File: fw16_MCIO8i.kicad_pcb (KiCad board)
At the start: 4 copper layers, 118.7 x 72.5 mm, 18 parts, among them U1 M24C32-FDW6TP

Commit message: Fixups
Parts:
- C1: value 0.1uF -> 1uF
- FAN_L1, FAN_R1: value FAN -> 59453-041110EDHLF
- MCIO1: value G97R22322HR -> G97R22312HR; footprint mcio-connector:AMPHENOL_G97R22322HR -> mcio-connector:AMPHENOL_G97R22312HR
- R1, R2: value 330 -> 330kΩ
- R3, R50, R51: value 10K -> 10kΩ
- R4: value 100k -> 100kΩ
- TP3, TP5: footprint TestPoint:TestPoint_Pad_D1.0mm -> TestPoint:TestPoint_Pad_D3.0mm
- moved MCIO1 0.56 mm to (134.2, 31.2)
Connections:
- FXBeam1 pad SA5: unconnected-(FXBeam1-PEX_RST#-PadSA5) -> /PEX_RST
- FXBeam1 pad SC2: unconnected-(FXBeam1-PEX_REFCLK-PadSC2) -> /PEX_CLK+
- FXBeam1 pad SD2: unconnected-(FXBeam1-PEX_REFCLK#-PadSD2) -> /PEX_CLK-
- MCIO1 pad A11: unconnected-(MCIO1-PCI0_RST-PadA11) -> /PEX_CLK+
- MCIO1 pad A12: unconnected-(MCIO1-PadA12) -> /PEX_CLK-
- MCIO1 pad A14: /TX2+ -> /RX2+
- MCIO1 pad A15: /TX2- -> /RX2-
- MCIO1 pad A17: /TX3+ -> /RX3+
- MCIO1 pad A18: /TX3- -> /RX3-
- MCIO1 pad A2: /TX0+ -> /RX0+
- MCIO1 pad A20: /TX4+ -> /RX4+
- MCIO1 pad A21: /TX4- -> /RX4-
- MCIO1 pad A23: /TX5+ -> /RX5+
- MCIO1 pad A24: /TX5- -> /RX5-
- MCIO1 pad A3: /TX0- -> /RX0-
- MCIO1 pad A32: /TX6+ -> /RX6+
- MCIO1 pad A33: /TX6- -> /RX6-
- MCIO1 pad A35: /TX7+ -> /RX7+
- MCIO1 pad A36: /TX7- -> /RX7-
- MCIO1 pad A5: /TX1+ -> /RX1+
- MCIO1 pad A6: /TX1- -> /RX1-
- MCIO1 pad B11: unconnected-(MCIO1-CLK0+-PadB11) -> /PEX_RST
- MCIO1 pad B14: /RX2+ -> /TX2+
- MCIO1 pad B15: /RX2- -> /TX2-
- MCIO1 pad B17: /RX3+ -> /TX3+
- MCIO1 pad B18: /RX3- -> /TX3-
- MCIO1 pad B2: /RX0+ -> /TX0+
- MCIO1 pad B20: /RX4+ -> /TX4+
- MCIO1 pad B21: /RX4- -> /TX4-
- MCIO1 pad B23: /RX5+ -> /TX5+
- MCIO1 pad B24: /RX5- -> /TX5-
- MCIO1 pad B3: /RX0- -> /TX0-
- MCIO1 pad B32: /RX6+ -> /TX6+
- MCIO1 pad B33: /RX6- -> /TX6-
- MCIO1 pad B35: /RX7+ -> /TX7+
- MCIO1 pad B36: /RX7- -> /TX7-
- MCIO1 pad B5: /RX1+ -> /TX1+
- MCIO1 pad B6: /RX1- -> /TX1-
- R1 pad 2: Net-(FXBeam1-ID0) -> Net-(R1-Pad2)
- R2 pad 2: Net-(FXBeam1-ID1) -> Net-(R2-Pad2)
- R3 pad 2: Net-(U1-WC) -> Net-(R3-Pad2)
- R4 pad 2: Net-(U1-WC) -> Net-(R3-Pad2)
- TP3 pad 1: Net-(FXBeam1-ID1) -> Net-(R2-Pad2)
- TP5 pad 1: Net-(FXBeam1-ID0) -> Net-(R1-Pad2)
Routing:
- net unconnected-(FXBeam1-PEX_RST#-PadSA5): track 33.0 -> 0.00 mm, vias 1 -> 0
- net /PEX_RST: track 0.00 -> 33.0 mm, vias 0 -> 1

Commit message: Fox
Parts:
- moved R2 65.7 mm to (144.7, 84.5), turned to 180 degrees
- moved TP3 59.4 mm to (141.0, 84.5)
- moved R1 57.2 mm to (78.5, 85.5)
- moved TP5 49.2 mm to (82.2, 85.5)
- moved C1 2.02 mm to (87.2, 75.8)
- moved R3 2.02 mm to (87.2, 77.0)
- moved R4 2.02 mm to (87.2, 78.0)
- moved R50 2.02 mm to (87.2, 79.2)
- moved R51 2.02 mm to (87.2, 80.2)
- renumbered U1 to EEPROM1, FXBeam1 to FXBEAM1
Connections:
- FXBEAM1 pad PJ1: Net-(FXBeam1-ID0) -> Net-(FXBEAM1-ID0)
- FXBEAM1 pad SL2: Net-(FXBeam1-ID1) -> Net-(FXBEAM1-ID1)
- R1 pad 2: Net-(R1-Pad2) -> Net-(FXBEAM1-ID0)
- R2 pad 2: Net-(R2-Pad2) -> Net-(FXBEAM1-ID1)
- TP3 pad 1: Net-(R2-Pad2) -> Net-(FXBEAM1-ID1)
- TP5 pad 1: Net-(R1-Pad2) -> Net-(FXBEAM1-ID0)
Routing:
- net GND: track 0.00 -> 818.4 mm, vias 0 -> 9
- net 12V_FAN: track 116.6 -> 0.00 mm
- net /RX1-: track 7.09 -> 68.3 mm, vias 1 -> 0
- net /RX1+: track 7.86 -> 68.2 mm, vias 1 -> 0
- net /TX0-: track 9.70 -> 68.2 mm, vias 0 -> 1
- net /TX0+: track 10.2 -> 68.2 mm, vias 0 -> 1
- net /RX2-: track 7.76 -> 64.0 mm
- net /RX2+: track 7.94 -> 64.0 mm
- net /FAN1_PWM: track 56.0 -> 0.00 mm, vias 2 -> 0
- net /RX0-: track 9.57 -> 65.4 mm
- net /TX5+: track 9.19 -> 64.9 mm
- net /RX3+: track 4.96 -> 60.6 mm
- net /RX3-: track 5.09 -> 60.5 mm
- net /RX0+: track 10.1 -> 63.9 mm
- net /FAN1_SPD: track 53.5 -> 0.00 mm, vias 2 -> 0
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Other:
- board text added: "Designed by Makuru and Love"
- board text removed: "Designed by Terrails"

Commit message: cat
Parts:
- removed R3: 10kΩ, PCM_JLCPCB:R_0402
- removed R4: 100kΩ, PCM_JLCPCB:R_0402
- moved C1 2.00 mm to (87.2, 77.8)
- moved EEPROM1 0.39 mm to (81.6, 78.8)
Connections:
- EEPROM1 pad 7: Net-(U1-WC) -> GND
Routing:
- net 12V_FAN: track 0.00 -> 111.4 mm, vias 0 -> 4
- net /FAN1_PWM: track 0.00 -> 59.5 mm
- net /FAN1_SPD: track 0.00 -> 57.3 mm, vias 0 -> 2
- net /FAN0_SPD: track 0.00 -> 51.6 mm, vias 0 -> 2
- net /PEX_RST: track 10.8 -> 62.0 mm
- net /FAN0_PWM: track 0.00 -> 46.1 mm, vias 0 -> 2
- net /TX6+: track 48.2 -> 83.7 mm, vias 1 -> 2
- net Net-(FXBEAM1-ID1): track 0.00 -> 34.9 mm, vias 0 -> 2
- net /TX6-: track 48.2 -> 82.3 mm, vias 1 -> 2
- net Net-(FXBEAM1-ID0): track 0.00 -> 32.7 mm, vias 0 -> 2
- net 3V3_ALW: track 0.00 -> 19.4 mm
- net /TX5+: track 64.9 -> 47.1 mm
- net /TX7+: track 43.4 -> 30.6 mm, vias 0 -> 1
- net /TX7-: track 43.3 -> 30.6 mm, vias 0 -> 1
- net /TX4-: track 57.9 -> 48.9 mm
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
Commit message: changed parts
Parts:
- FAN_L1, FAN_R1: value 59453-041110EDHLF -> F3011B7H111005E200; footprint fan-connector:AMPHENOL_59453-041110EDHLF -> fan-connector:AMPHENOL_F33D-1A7H1-E7C04
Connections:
- FAN_L1 pad 1: 12V_FAN -> GND
- FAN_L1 pad 2: /FAN0_SPD -> /FAN0_PWM
- FAN_L1 pad 3: /FAN0_PWM -> /FAN0_SPD
- FAN_L1 pad 4: GND -> 12V_FAN
- FAN_R1 pad 1: 12V_FAN -> GND
- FAN_R1 pad 2: /FAN1_SPD -> /FAN1_PWM
- FAN_R1 pad 3: /FAN1_PWM -> /FAN1_SPD
- FAN_R1 pad 4: GND -> 12V_FAN
- FXBEAM1 pad PC3: /I2C_SCL -> unconnected-(FXBEAM1-I2C_CLK_ALW-PadPC3)
- FXBEAM1 pad PF2: unconnected-(FXBEAM1-I2C_INT_ALW-PadPF2) -> /I2C_SCL
- FXBEAM1 pad PG2: unconnected-(FXBEAM1-I2C_INT_VS-PadPG2) -> /PE_SDA
- FXBEAM1 pad PG3: unconnected-(FXBEAM1-I2C_DAT_VS-PadPG3) -> /PE_SCL
- MCIO1 pad B8: unconnected-(MCIO1-SMSCL_A-PadB8) -> /PE_SCL
- MCIO1 pad B9: unconnected-(MCIO1-SMSDA_A-PadB9) -> /PE_SDA
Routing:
- net GND: track 821.0 -> 258.5 mm, vias 9 -> 36
- net /TX7-: track 30.6 -> 92.2 mm, vias 1 -> 2
- net /TX7+: track 30.6 -> 92.1 mm, vias 1 -> 2
- net /TX6+: track 83.7 -> 26.6 mm
- net /TX6-: track 82.3 -> 25.4 mm
- net /TX1+: track 0.00 -> 39.0 mm, vias 0 -> 1
- net /TX1-: track 0.00 -> 38.3 mm, vias 0 -> 1
- net /PEX_RST: track 62.0 -> 24.1 mm, vias 3 -> 1
- net /RX1-: track 68.3 -> 30.5 mm, vias 0 -> 1
- net /RX1+: track 68.2 -> 31.1 mm, vias 0 -> 1
- net /RX3-: track 60.5 -> 23.7 mm, vias 0 -> 1
- net /RX2-: track 64.0 -> 28.2 mm, vias 0 -> 1
- net /RX4+: track 55.5 -> 19.8 mm, vias 0 -> 1
- net /RX3+: track 60.5 -> 25.0 mm, vias 0 -> 1
- net /RX4-: track 55.5 -> 20.5 mm, vias 0 -> 1
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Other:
- board text added: "Designed by Makuru"
- board text removed: "Designed by Makuru and Love"

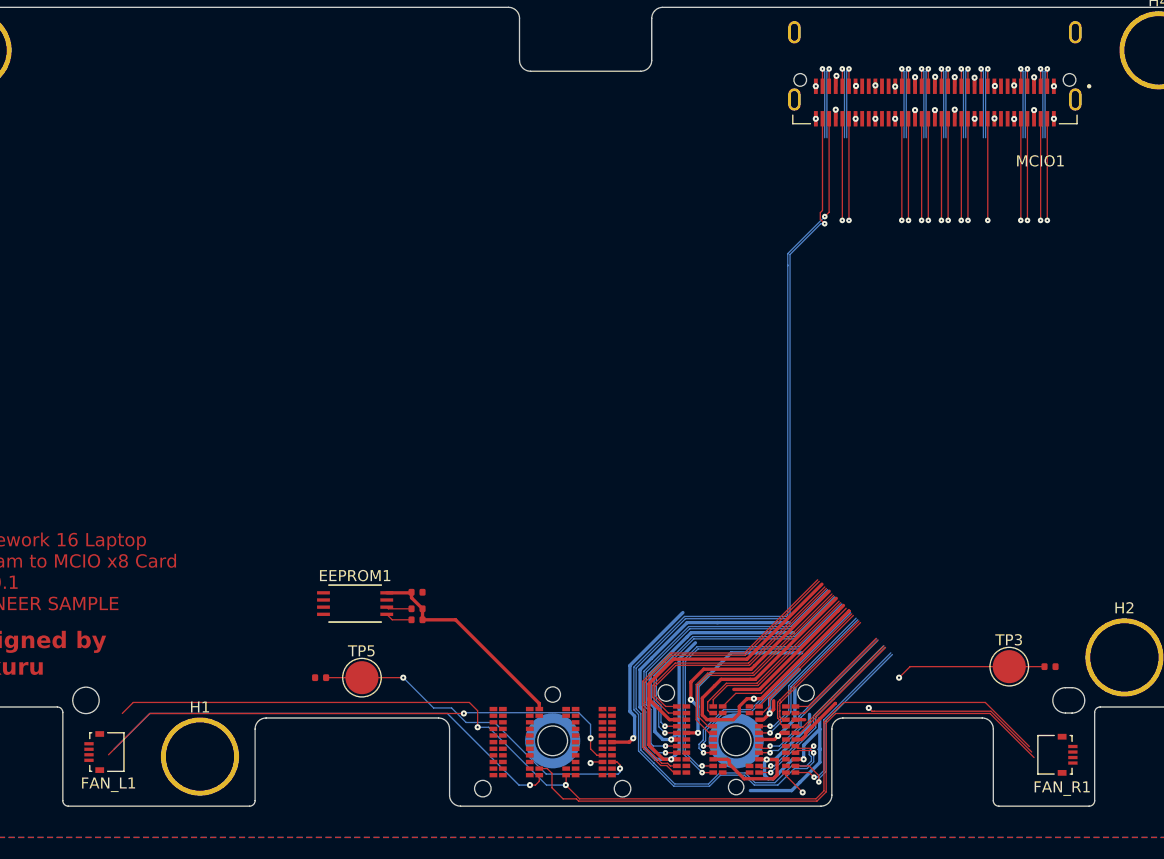
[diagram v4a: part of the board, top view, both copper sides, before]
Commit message: Rerouted fxbeam
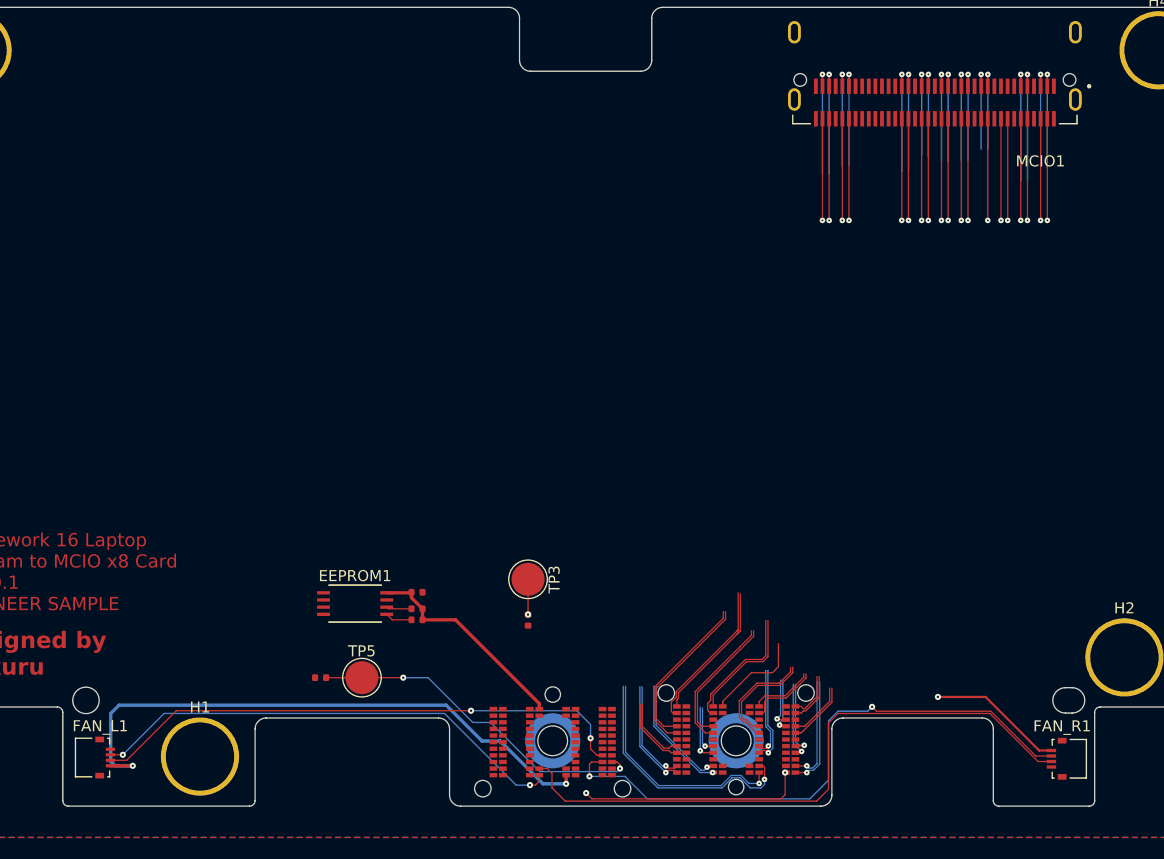
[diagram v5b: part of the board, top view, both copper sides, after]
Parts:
- moved R2 47.6 mm to (97.3, 80.3), turned to 90 degrees
- moved TP3 44.4 mm to (97.3, 76.6), turned to -90 degrees
- moved FAN_L1 0.50 mm to (58.5, 92.8), turned to -90 degrees
- moved FAN_R1 0.36 mm to (145.8, 92.9), turned to 90 degrees
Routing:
- net GND: track 258.5 -> 0.00 mm, vias 36 -> 0
- net /TX7-: track 92.2 -> 16.2 mm
- net /TX7+: track 92.1 -> 16.2 mm
- net /TX0+: track 38.8 -> 15.6 mm, vias 2 -> 1
- net /TX0-: track 38.0 -> 15.3 mm, vias 2 -> 1
- net /TX1+: track 39.0 -> 19.2 mm, vias 1 -> 2
- net /TX1-: track 38.3 -> 18.7 mm, vias 1 -> 2
- net /TX3+: track 37.7 -> 20.0 mm
- net /TX3-: track 37.0 -> 19.8 mm
- net /TX2+: track 29.4 -> 13.5 mm
- net /TX2-: track 30.2 -> 14.4 mm
- net Net-(FXBEAM1-ID1): track 34.9 -> 46.5 mm, vias 2 -> 3
- net 12V_FAN: track 97.1 -> 108.3 mm, vias 2 -> 3
- net /RX0+: track 34.1 -> 24.5 mm, vias 2 -> 1
- net /PE_SCL: track 0.00 -> 9.23 mm, vias 0 -> 1
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
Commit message: routed
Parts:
- moved MCIO1 57.4 mm to (76.8, 31.1)
- moved R2 53.6 mm to (45.1, 68.3), turned to 0 degrees
- moved TP3 48.2 mm to (49.8, 68.3), turned to 180 degrees
- moved R1 0.66 mm to (77.8, 85.5)
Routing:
- net /RX6-: track 14.0 -> 143.2 mm, vias 1 -> 4
- net /RX6+: track 13.7 -> 142.3 mm, vias 1 -> 4
- net /RX7-: track 15.4 -> 141.9 mm, vias 1 -> 4
- net /RX7+: track 15.9 -> 142.4 mm, vias 1 -> 4
- net /RX4-: track 14.9 -> 138.5 mm, vias 1 -> 4
- net /RX4+: track 14.4 -> 137.2 mm, vias 1 -> 4
- net /RX5+: track 19.4 -> 140.2 mm, vias 1 -> 4
- net /RX5-: track 19.9 -> 140.5 mm, vias 1 -> 4
- net /RX3+: track 20.9 -> 125.7 mm, vias 1 -> 2
- net /RX3-: track 19.7 -> 122.7 mm, vias 1 -> 2
- net /TX6-: track 19.2 -> 117.0 mm, vias 2 -> 4
- net /TX6+: track 18.9 -> 115.9 mm, vias 2 -> 4
- net /RX2-: track 20.8 -> 116.2 mm, vias 1 -> 2
- net /RX2+: track 21.3 -> 115.6 mm, vias 1 -> 2
- net /PE_SCL: track 9.23 -> 91.9 mm, vias 1 -> 2
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
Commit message: Fixed errors
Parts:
- removed H1, H2, H3, H4: MountingHole_Pad, expansion_bay:MountingHole_6.2mm
- renumbered TP5 to TP_POWER1, TP3 to TP_SIGNAL1
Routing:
- net /RX3+: track 125.7 -> 122.5 mm
- net /TX4-: track 90.7 -> 92.9 mm
- net /TX5-: track 86.0 -> 87.7 mm
- net /PEX_CLK+: track 79.6 -> 81.2 mm
- net /RX6+: track 142.3 -> 143.7 mm
- net /RX4+: track 137.2 -> 138.4 mm
- net /TX0-: track 70.2 -> 71.3 mm
- net /TX6+: track 115.9 -> 117.0 mm
- net /TX7+: track 93.1 -> 93.8 mm
- net /TX3+: track 84.3 -> 85.0 mm
- net /FAN1_SPD: track 53.6 -> 54.3 mm
- net /TX2+: track 80.8 -> 81.4 mm
- net /RX6-: track 143.2 -> 143.8 mm
- net /TX3-: track 84.4 -> 85.0 mm
- net /TX1-: track 72.2 -> 72.7 mm
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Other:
- outline, holes or cut-outs redrawn

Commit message: New routing
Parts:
- IN1: renamed from FXBEAM1; value IN -> FXBEAM
- moved EEPROM1 0.50 mm to (81.1, 78.8)
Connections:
- IN1 pad PC3: unconnected-(FXBEAM1-I2C_CLK_ALW-PadPC3) -> /I2C_SDA
- IN1 pad PD3: /I2C_SDA -> /I2C_SCL
- IN1 pad PF2: /I2C_SCL -> unconnected-(IN1-I2C_INT_ALW-PadPF2)
- IN1 pad PF3: unconnected-(FXBEAM1-I2C_CLK_VS-PadPF3) -> /PEX_RST
- IN1 pad PG2: /PE_SDA -> unconnected-(IN1-PEX_CLK_REQ-PadPG2)
- IN1 pad PG3: /PE_SCL -> unconnected-(IN1-PEX2_RST-PadPG3)
- IN1 pad PK1: unconnected-(FXBEAM1-DDS_SDA-PadPK1) -> /PE_SCL
- IN1 pad PL2: unconnected-(FXBEAM1-DDS_CLK-PadPL2) -> /PE_SDA
- IN1 pad SA5: /PEX_RST -> unconnected-(IN1-PEX_RST#-PadSA5)
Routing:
- net /RX4+: track 138.4 -> 90.8 mm, vias 4 -> 2
- net /RX4-: track 138.5 -> 91.5 mm, vias 4 -> 2
- net /PE_SDA: track 89.2 -> 129.0 mm, vias 2 -> 4
- net /PE_SCL: track 92.1 -> 125.8 mm, vias 2 -> 4
- net /TX1-: track 72.7 -> 103.0 mm, vias 4 -> 2
- net /TX1+: track 72.7 -> 102.4 mm, vias 4 -> 2
- net /TX4+: track 93.0 -> 120.7 mm, vias 2 -> 4
- net /TX4-: track 92.9 -> 118.7 mm, vias 2 -> 4
- net /TX0+: track 71.4 -> 96.1 mm, vias 4 -> 2
- net /TX0-: track 71.3 -> 94.9 mm, vias 4 -> 2
- net /TX6+: track 117.0 -> 101.6 mm, vias 4 -> 2
- net /RX1-: track 95.9 -> 80.7 mm
- net /RX1+: track 95.9 -> 81.2 mm
- net /TX6-: track 117.0 -> 102.4 mm, vias 4 -> 2
- net /RX2+: track 116.1 -> 106.0 mm
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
